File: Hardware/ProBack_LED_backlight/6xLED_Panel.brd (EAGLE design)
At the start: 48 x 6 mm, 17 parts

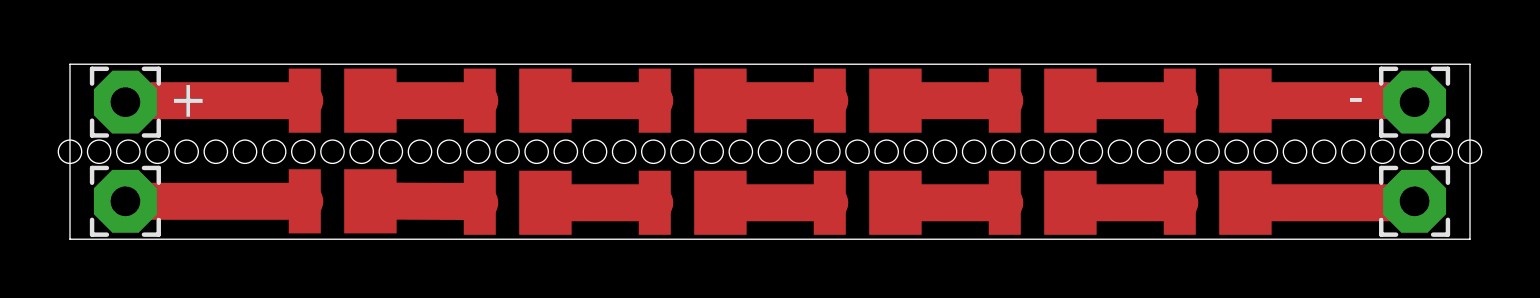
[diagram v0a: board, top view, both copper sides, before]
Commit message: Updated for PCBWay of doing boards
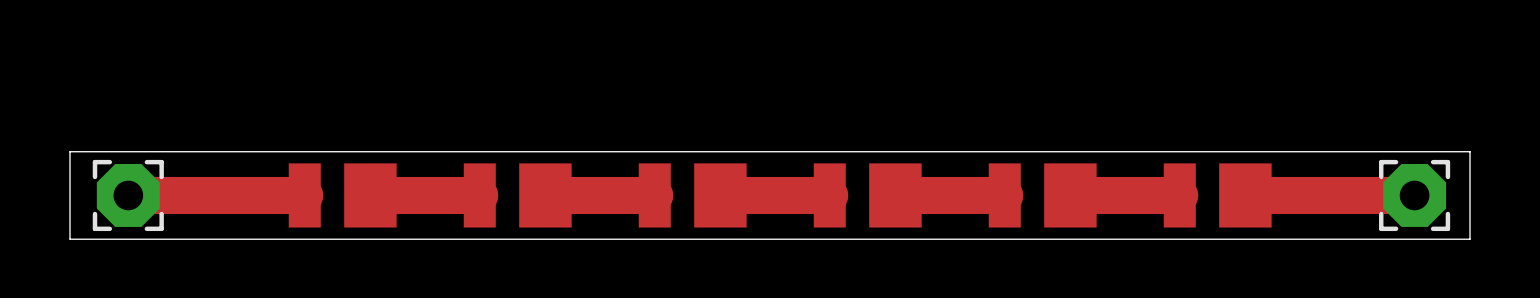
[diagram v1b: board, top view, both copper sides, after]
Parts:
- removed D10, D11, D12, D7, D8, D9: YUJI_2835_SMD, Yuji_LED:2835_SMD
- removed PAD1, PAD3: WIREPAD1,6/0,9, wirepad:2,15/1,0
- removed PAD2, PAD4: (no value), wirepad:2,15/1,0
- added +: WIREPAD1,6/0,9, wirepad:2,15/1,0
- added -: (no value), wirepad:2,15/1,0
- moved D2 0.25 mm to (15.0, 1.50)
- moved D3 0.25 mm to (21.0, 1.50)
- moved D4 0.25 mm to (27.0, 1.50)
- moved D5 0.25 mm to (33.0, 1.50)
- moved D6 0.25 mm to (39.0, 1.50)
- moved D1 0.20 mm to (9.00, 1.50)
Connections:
- removed net N$12: D10.ANODE, D9.CATHODE
- removed net N$13: D10.CATHODE, D11.ANODE
- removed net N$14: D11.CATHODE, D12.ANODE
- removed net N$5: D7.CATHODE, D8.ANODE
- removed net N$6: D7.ANODE, PAD3.1
- removed net N$7: D8.CATHODE, D9.ANODE
- removed net N$8: D12.CATHODE, PAD4.1
- net N$2: now also +.1; no longer PAD1.1
- net N$4: now also -.1; no longer PAD2.1
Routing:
- net N$6: track 6.17 -> 0.00 mm
- net N$8: track 5.82 -> 0.00 mm
- net N$7: track 3.75 -> 0.00 mm
- net N$5: track 3.75 -> 0.00 mm
- net N$14: track 3.75 -> 0.00 mm
- net N$12: track 3.75 -> 0.00 mm
- net N$13: track 3.75 -> 0.00 mm
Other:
- board size 48 x 6 mm -> 48 x 3 mm
- board text removed: "- LED"
- board text removed: "-LED"
- board text removed: "LED +"
- board text removed: "LED+"
